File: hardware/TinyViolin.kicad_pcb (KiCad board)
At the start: 2 copper layers, 100 x 80 mm, 46 parts, among them J1 AVR-ISP-6, J2 503182-1852, SW1 SW_SPDT, SW2 Tactile, SW3 SW_Push, SW4 SW_Push, SW5 SW_Push, SW6 SW_Push, U1 ATmega328-PU, U2 TPS613222ADBVT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

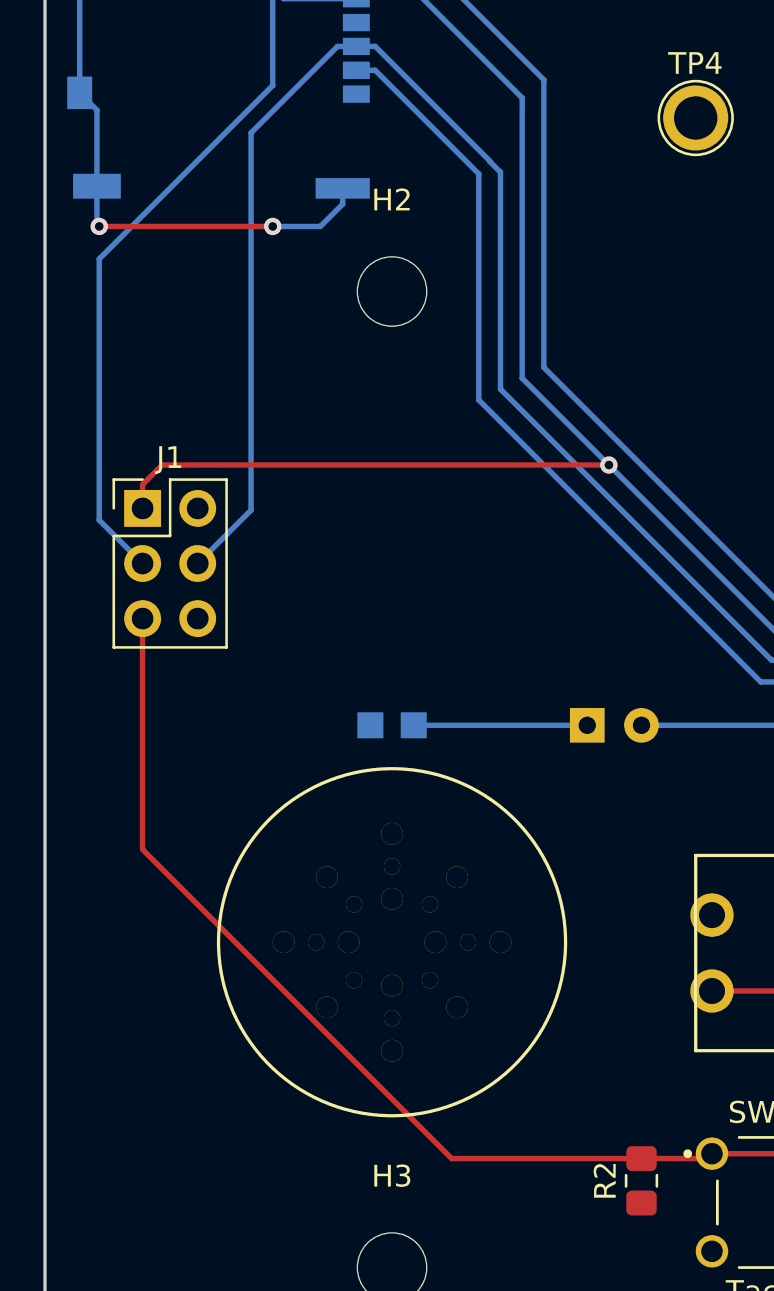
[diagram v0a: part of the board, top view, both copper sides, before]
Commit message: Moved icsp header up
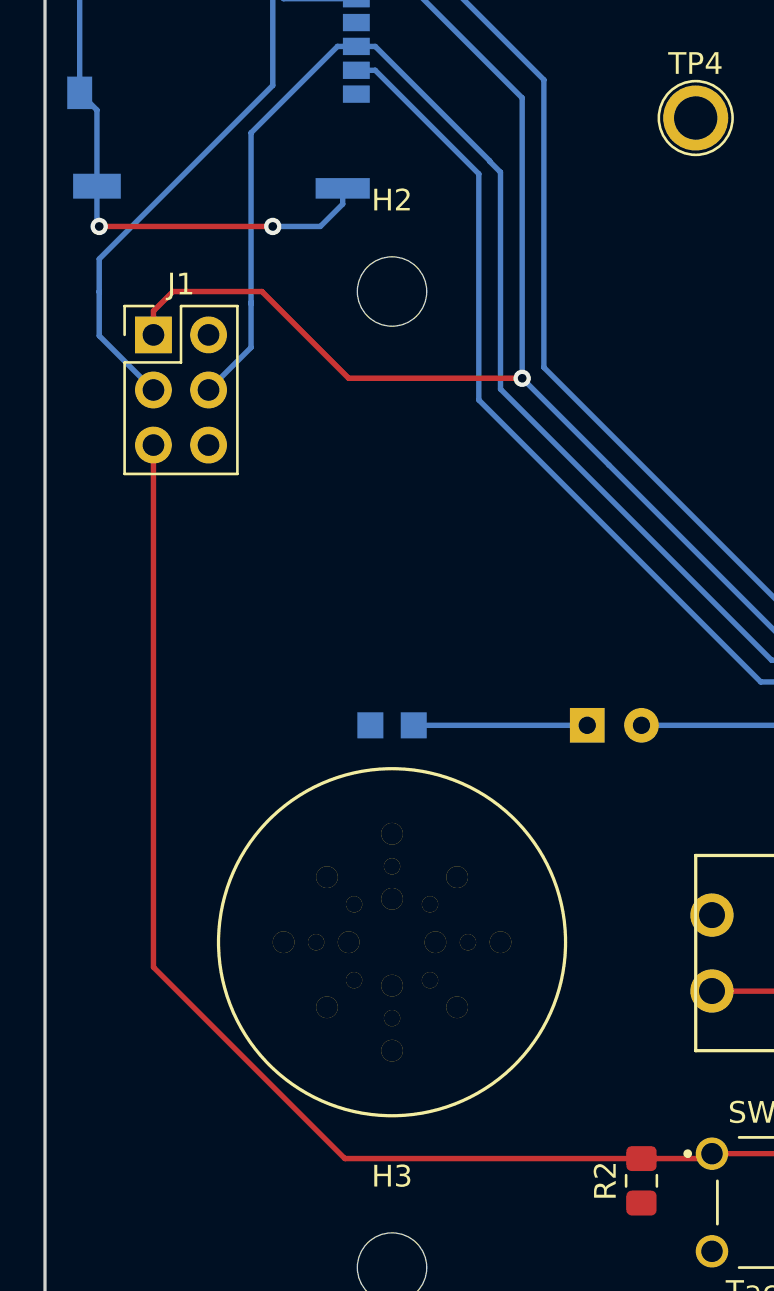
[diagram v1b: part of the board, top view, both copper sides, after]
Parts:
- moved J1 8.02 mm to (25.0, 52.0)
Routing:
- net /~RST: track 104.1 -> 115.3 mm
- net /MOSI: track 77.7 -> 69.6 mm
- net /SCK: track 101.9 -> 94.2 mm
- net /MISO: track 79.0 -> 76.1 mm
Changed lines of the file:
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@@
     (thickness 1.6)
     (drawings 4)
-    (tracks 158)
+    (tracks 163)
     (zones 0)
     (modules 46)
@@
   )
   (module Connector_PinHeader_2.54mm:PinHeader_2x03_P2.54mm_Vertical (layer F.Cu)
-    (at 24.5 60)
+    (at 25 52)
     (descr "Through hole straight pin header, 2x03, 2.54mm pitch, double rows")
     (tags "Through hole pin header THT 2x03 2.54mm double row")
@@
   (segment (start 33.485 38.7) (end 29.5 42.685) (width 0.25) (layer B.Cu) (net 1))
   (segment (start 34.355 38.7) (end 33.485 38.7) (width 0.25) (layer B.Cu) (net 1))
-  (segment (start 29.5 60.08) (end 27.04 62.54) (width 0.25) (layer B.Cu) (net 1))
-  (segment (start 29.5 42.685) (end 29.5 60.08) (width 0.25) (layer B.Cu) (net 1))
+  (segment (start 29.5 50.58) (end 29.5 50.5) (width 0.25) (layer B.Cu) (net 1))
+  (segment (start 29.5 42.685) (end 29.5 50.5) (width 0.25) (layer B.Cu) (net 1))
+  (segment (start 27.54 54.54) (end 29.5 52.58) (width 0.25) (layer B.Cu) (net 1))
+  (segment (start 29.5 52.58) (end 29.5 50.5) (width 0.25) (layer B.Cu) (net 1))
   (via (at 95 62) (size 0.8) (drill 0.4) (layers F.Cu B.Cu) (net 11))
   (via (at 95 73) (size 0.8) (drill 0.4) (layers F.Cu B.Cu) (net 11))
@@
   (segment (start 42 54) (end 42 41.075) (width 0.25) (layer B.Cu) (net 5))
   (segment (start 42 41.075) (end 35.225 34.3) (width 0.25) (layer B.Cu) (net 5))
-  (segment (start 24.5 58.9) (end 25.4 58) (width 0.25) (layer F.Cu) (net 5))
-  (segment (start 24.5 60) (end 24.5 58.9) (width 0.25) (layer F.Cu) (net 5))
-  (segment (start 25.4 58) (end 46 58) (width 0.25) (layer F.Cu) (net 5))
   (segment (start 46 58) (end 42 54) (width 0.25) (layer B.Cu) (net 5))
-  (via (at 46 58) (size 0.8) (drill 0.4) (layers F.Cu B.Cu) (net 5))
+  (via (at 42 54) (size 0.8) (drill 0.4) (layers F.Cu B.Cu) (net 5))
+  (segment (start 42 54) (end 34 54) (width 0.25) (layer F.Cu) (net 5))
+  (segment (start 25 50.9) (end 25.9 50) (width 0.25) (layer F.Cu) (net 5))
+  (segment (start 25 52) (end 25 50.9) (width 0.25) (layer F.Cu) (net 5))
+  (segment (start 25.9 50) (end 30 50) (width 0.25) (layer F.Cu) (net 5))
+  (segment (start 34 54) (end 30 50) (width 0.25) (layer F.Cu) (net 5))
   (segment (start 69.64 70.12) (end 69.64 70.52) (width 0.25) (layer B.Cu) (net 6))
   (segment (start 69.64 69.72) (end 69.64 70.12) (width 0.25) (layer B.Cu) (net 6))
-  (segment (start 22.5 60.54) (end 24.5 62.54) (width 0.25) (layer B.Cu) (net 6))
-  (segment (start 22.5 48.5) (end 22.5 60.54) (width 0.25) (layer B.Cu) (net 6))
   (segment (start 33 32) (end 30.5 34.5) (width 0.25) (layer B.Cu) (net 6))
   (segment (start 34.760002 32) (end 33 32) (width 0.25) (layer B.Cu) (net 6))
@@
   (segment (start 30.5 36) (end 30.5 40.5) (width 0.25) (layer B.Cu) (net 6))
   (segment (start 30.5 40.5) (end 22.5 48.5) (width 0.25) (layer B.Cu) (net 6))
+  (segment (start 22.5 50.04) (end 22.5 50) (width 0.25) (layer B.Cu) (net 6))
+  (segment (start 22.5 48.5) (end 22.5 50) (width 0.25) (layer B.Cu) (net 6))
+  (segment (start 22.5 52.04) (end 25 54.54) (width 0.25) (layer B.Cu) (net 6))
+  (segment (start 22.5 50) (end 22.5 52.04) (width 0.25) (layer B.Cu) (net 6))
   (segment (start 79.8 61.05) (end 71.25 52.5) (width 0.25) (layer B.Cu) (net 7))
   (segment (start 79.8 62.5) (end 79.8 61.05) (width 0.25) (layer B.Cu) (net 7))
@@
   (segment (start 47.5 89.975) (end 50.525 89.975) (width 0.25) (layer F.Cu) (net 14))
   (segment (start 50.75 89.75) (end 57.25 89.75) (width 0.25) (layer F.Cu) (net 14))
-  (segment (start 46.7 89.975) (end 47.5 89.975) (width 0.25) (layer F.Cu) (net 14))
-  (segment (start 38.753998 89.975) (end 46.7 89.975) (width 0.25) (layer F.Cu) (net 14))
-  (segment (start 24.5 75.721002) (end 38.753998 89.975) (width 0.25) (layer F.Cu) (net 14))
-  (segment (start 24.5 65.58) (end 24.5 75.721002) (width 0.25) (layer F.Cu) (net 14))
   (segment (start 93.55 62.5) (end 94.5 63.45) (width 0.25) (layer B.Cu) (net 14))
   (segment (start 92.5 62.5) (end 93.55 62.5) (width 0.25) (layer B.Cu) (net 14))
@@
   (segment (start 67 80) (end 57.25 89.75) (width 0.25) (layer B.Cu) (net 14))
   (segment (start 86 80) (end 67 80) (width 0.25) (layer B.Cu) (net 14))
+  (segment (start 25 57.08) (end 25 81.150998) (width 0.25) (layer F.Cu) (net 14))
+  (segment (start 33.824002 89.975) (end 25 81.150998) (width 0.25) (layer F.Cu) (net 14))
+  (segment (start 47.5 89.975) (end 33.824002 89.975) (width 0.25) (layer F.Cu) (net 14))
   (segment (start 98.475 70) (end 103.5 70) (width 0.25) (layer F.Cu) (net 15))
   (segment (start 97 68.525) (end 98.475 70) (width 0.25) (layer F.Cu) (net 15))

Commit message: Fixed labels
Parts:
- J1: value AVR-ISP-6 -> ICSP
- U2: value TPS613222ADBVT -> BOOST
- U3: value MIC5504-3.3YM5 -> REG
- moved C10 2.50 mm to (47.5, 70.0), turned to 180 degrees
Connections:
- C10 pad 1: Net-(C10-Pad1) -> /SPEAKER
- C10 pad 2: /SPEAKER -> Net-(C10-Pad2)
- LS1 pad 1: Net-(C10-Pad1) -> Net-(C10-Pad2)
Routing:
- net Net-(C10-Pad2): track 0.00 -> 8.00 mm
- net Net-(C10-Pad1): track 8.00 -> 0.00 mm
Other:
- board text added: "+"
- board text added: "-"
- board text added: "."
- board text added: "Tiny Violin MM v1.0"

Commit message: Wrote code for buttons and leds
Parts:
- U1: footprint Package_DIP:DIP-28_W7.62mm_Socket_LongPads -> Package_DIP:DIP-28_W7.62mm_LongPads

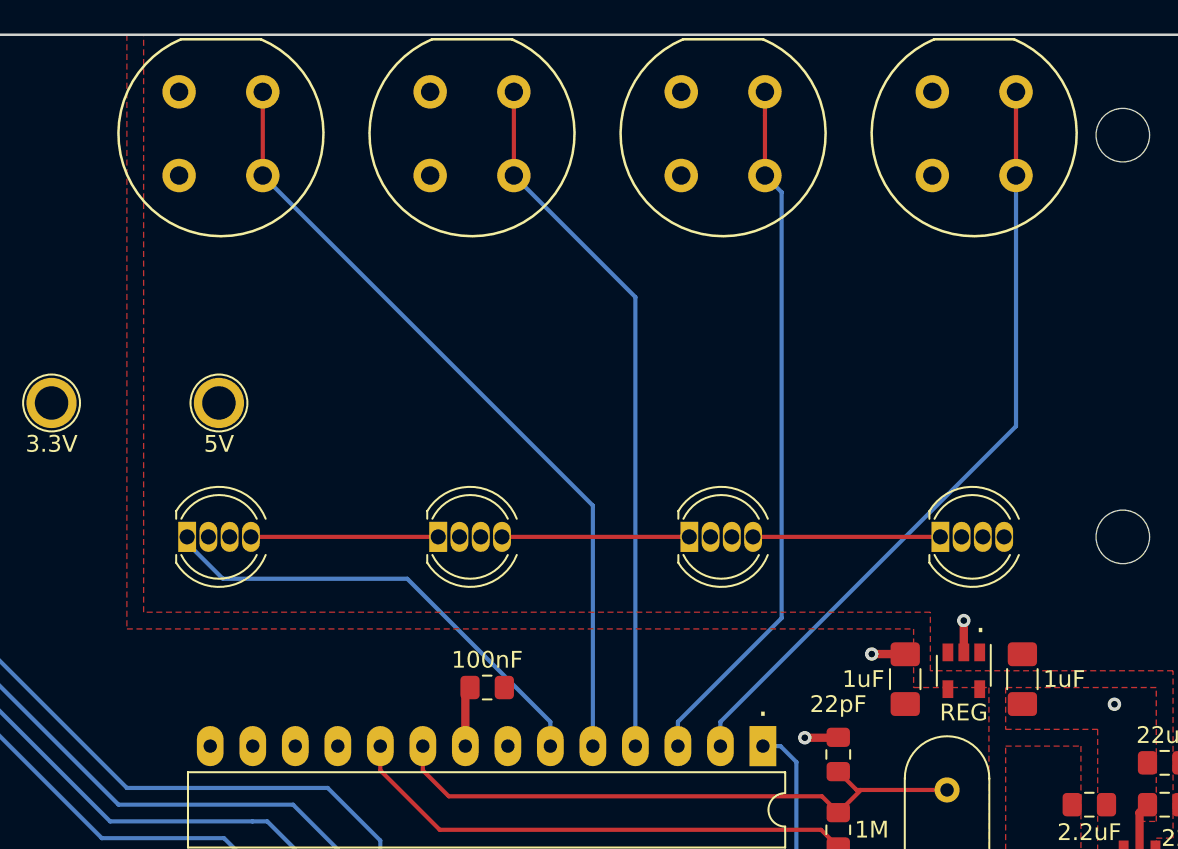
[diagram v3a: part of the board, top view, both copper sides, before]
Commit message: Moved holes and leds 1mm to the left
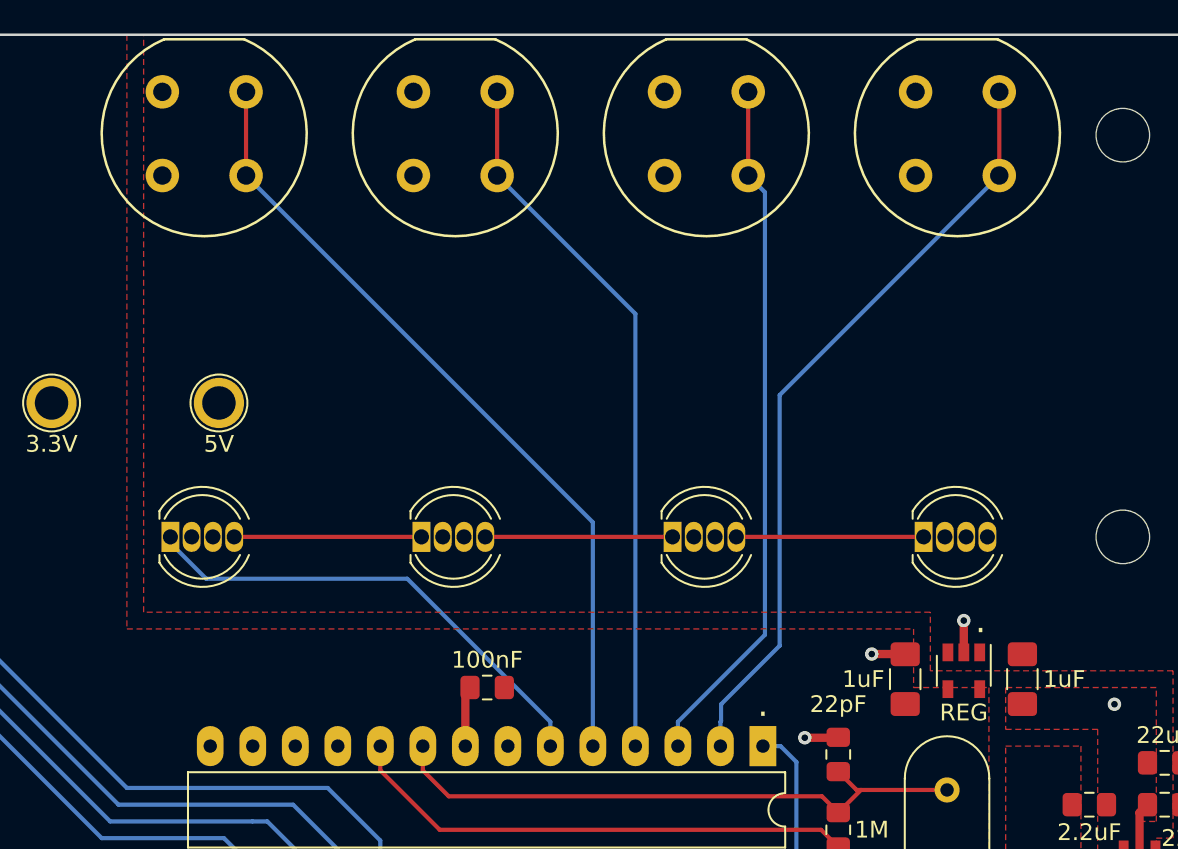
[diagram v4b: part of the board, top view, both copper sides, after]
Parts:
- moved D3 1.00 mm to (57.1, 50.0)
- moved D4 1.00 mm to (72.1, 50.0)
- moved D5 1.00 mm to (87.1, 50.0)
- moved D6 1.00 mm to (102.1, 50.0)
- moved SW3 1.00 mm to (61.5, 23.5)
- moved SW4 1.00 mm to (76.5, 23.5)
- moved SW5 1.00 mm to (91.5, 23.5)
- moved SW6 1.00 mm to (106.5, 23.5)
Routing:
- net /LEDS: track 27.9 -> 28.9 mm
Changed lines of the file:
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@@
     (thickness 1.6)
     (drawings 11)
-    (tracks 163)
+    (tracks 164)
     (zones 0)
     (modules 46)
@@
   )
   (module D6:D6 (layer F.Cu)
-    (at 107.5 23.5 270)
+    (at 106.5 23.5 270)
     (fp_text reference SW6 (at 6 9.5 270) (layer F.SilkS) hide
       (effects (font (size 1 1) (thickness 0.15)))
@@
   )
   (module D6:D6 (layer F.Cu)
-    (at 92.5 23.5 270)
+    (at 91.5 23.5 270)
     (fp_text reference SW5 (at 6 9.5 270) (layer F.SilkS) hide
       (effects (font (size 1 1) (thickness 0.15)))
@@
   )
   (module D6:D6 (layer F.Cu)
-    (at 77.5 23.5 270)
+    (at 76.5 23.5 270)
     (fp_text reference SW4 (at 6 9.5 270) (layer F.SilkS) hide
       (effects (font (size 1 1) (thickness 0.15)))
@@
   )
   (module D6:D6 (layer F.Cu)
-    (at 62.5 23.5 270)
+    (at 61.5 23.5 270)
     (fp_text reference SW3 (at 6 9.5 270) (layer F.SilkS) hide
       (effects (font (size 1 1) (thickness 0.15)))
@@
   )
   (module LED_THT:LED_D5.0mm-4_RGB (layer F.Cu)
-    (at 73.1 50)
+    (at 72.1 50)
     (descr "LED, diameter 5.0mm, 2 pins, diameter 5.0mm, 3 pins, diameter 5.0mm, 4 pins, http://www.kingbright.com/attachments/file/psearch/000/00/00/L-154A4SUREQBFZGEW(Ver.9A).pdf")
     (tags "LED diameter 5.0mm 2 pins diameter 5.0mm 3 pins diameter 5.0mm 4 pins RGB RGBLED")
@@
   )
   (module LED_THT:LED_D5.0mm-4_RGB (layer F.Cu)
-    (at 58.1 50)
+    (at 57.1 50)
     (descr "LED, diameter 5.0mm, 2 pins, diameter 5.0mm, 3 pins, diameter 5.0mm, 4 pins, http://www.kingbright.com/attachments/file/psearch/000/00/00/L-154A4SUREQBFZGEW(Ver.9A).pdf")
     (tags "LED diameter 5.0mm 2 pins diameter 5.0mm 3 pins diameter 5.0mm 4 pins RGB RGBLED")
@@
   )
   (module LED_THT:LED_D5.0mm-4_RGB (layer F.Cu)
-    (at 103.1 50)
+    (at 102.1 50)
     (descr "LED, diameter 5.0mm, 2 pins, diameter 5.0mm, 3 pins, diameter 5.0mm, 4 pins, http://www.kingbright.com/attachments/file/psearch/000/00/00/L-154A4SUREQBFZGEW(Ver.9A).pdf")
     (tags "LED diameter 5.0mm 2 pins diameter 5.0mm 3 pins diameter 5.0mm 4 pins RGB RGBLED")
@@
   )
   (module LED_THT:LED_D5.0mm-4_RGB (layer F.Cu)
-    (at 88.1 50)
+    (at 87.1 50)
     (descr "LED, diameter 5.0mm, 2 pins, diameter 5.0mm, 3 pins, diameter 5.0mm, 4 pins, http://www.kingbright.com/attachments/file/psearch/000/00/00/L-154A4SUREQBFZGEW(Ver.9A).pdf")
     (tags "LED diameter 5.0mm 2 pins diameter 5.0mm 3 pins diameter 5.0mm 4 pins RGB RGBLED")
@@
   (segment (start 22.5 52.04) (end 25 54.54) (width 0.25) (layer B.Cu) (net 6))
   (segment (start 22.5 50) (end 22.5 52.04) (width 0.25) (layer B.Cu) (net 6))
+  (segment (start 58.1 50.365) (end 58.1 50) (width 0.25) (layer B.Cu) (net 3))
+  (segment (start 57.1 50.365) (end 57.1 50) (width 0.25) (layer B.Cu) (net 7))
+  (segment (start 59.235 52.5) (end 57.1 50.365) (width 0.25) (layer B.Cu) (net 7))
+  (segment (start 71.25 52.5) (end 59.235 52.5) (width 0.25) (layer B.Cu) (net 7))
   (segment (start 79.8 61.05) (end 71.25 52.5) (width 0.25) (layer B.Cu) (net 7))
   (segment (start 79.8 62.5) (end 79.8 61.05) (width 0.25) (layer B.Cu) (net 7))
-  (segment (start 58.1 50.365) (end 58.1 50) (width 0.25) (layer B.Cu) (net 7))
-  (segment (start 60.235 52.5) (end 58.1 50.365) (width 0.25) (layer B.Cu) (net 7))
-  (segment (start 71.25 52.5) (end 60.235 52.5) (width 0.25) (layer B.Cu) (net 7))
   (segment (start 79.8 70.52) (end 79.8 70.12) (width 0.25) (layer F.Cu) (net 8))
   (segment (start 68.07 82.25) (end 79.8 70.52) (width 0.25) (layer F.Cu) (net 8))
@@
   (segment (start 95.975 67.5) (end 97 68.525) (width 0.25) (layer F.Cu) (net 14))
   (segment (start 73.19 67.5) (end 95.975 67.5) (width 0.25) (layer F.Cu) (net 14))
-  (segment (start 107.619299 29.825612) (end 107.619299 28.411399) (width 0.25) (layer B.Cu) (net 16))
-  (segment (start 107.619299 43.390701) (end 107.619299 29.825612) (width 0.25) (layer B.Cu) (net 16))
-  (segment (start 89.96 61.05) (end 107.619299 43.390701) (width 0.25) (layer B.Cu) (net 16))
+  (segment (start 89.96 61.05) (end 90 61.01) (width 0.25) (layer B.Cu) (net 16))
   (segment (start 89.96 62.5) (end 89.96 61.05) (width 0.25) (layer B.Cu) (net 16))
-  (segment (start 107.619299 24.825612) (end 107.619299 28.411399) (width 0.25) (layer F.Cu) (net 16))
-  (segment (start 107.619299 23.411399) (end 107.619299 24.825612) (width 0.25) (layer F.Cu) (net 16))
+  (segment (start 90 61.01) (end 90 60) (width 0.25) (layer B.Cu) (net 16))
+  (segment (start 90 60) (end 93.5 56.5) (width 0.25) (layer B.Cu) (net 16))
+  (segment (start 93.5 41.530698) (end 106.619299 28.411399) (width 0.25) (layer B.Cu) (net 16))
+  (segment (start 93.5 56.5) (end 93.5 41.530698) (width 0.25) (layer B.Cu) (net 16))
+  (segment (start 106.619299 28.411399) (end 106.619299 23.411399) (width 0.25) (layer F.Cu) (net 16))
   (segment (start 67.1 62.5) (end 67.1 62.9) (width 0.25) (layer F.Cu) (net 17))
-  (segment (start 82.34 48.1321) (end 62.619299 28.411399) (width 0.25) (layer B.Cu) (net 25))
-  (segment (start 82.34 62.5) (end 82.34 48.1321) (width 0.25) (layer B.Cu) (net 25))
-  (segment (start 62.619299 23.411399) (end 62.619299 28.411399) (width 0.25) (layer F.Cu) (net 25))
-  (segment (start 84.88 35.6721) (end 77.619299 28.411399) (width 0.25) (layer B.Cu) (net 26))
-  (segment (start 84.88 62.5) (end 84.88 35.6721) (width 0.25) (layer B.Cu) (net 26))
-  (segment (start 77.619299 23.411399) (end 77.619299 28.411399) (width 0.25) (layer F.Cu) (net 26))
-  (segment (start 93.619298 29.411398) (end 92.619299 28.411399) (width 0.25) (layer B.Cu) (net 27))
-  (segment (start 93.619298 54.850702) (end 93.619298 29.411398) (width 0.25) (layer B.Cu) (net 27))
-  (segment (start 87.42 61.05) (end 93.619298 54.850702) (width 0.25) (layer B.Cu) (net 27))
+  (segment (start 82.34 49.1321) (end 82.34 62.5) (width 0.25) (layer B.Cu) (net 25))
+  (segment (start 61.619299 28.411399) (end 82.34 49.1321) (width 0.25) (layer B.Cu) (net 25))
+  (segment (start 61.619299 28.411399) (end 61.619299 23.411399) (width 0.25) (layer F.Cu) (net 25))
+  (segment (start 84.88 36.6721) (end 76.619299 28.411399) (width 0.25) (layer B.Cu) (net 26))
+  (segment (start 84.88 62.5) (end 84.88 36.6721) (width 0.25) (layer B.Cu) (net 26))
+  (segment (start 76.619299 28.411399) (end 76.619299 23.411399) (width 0.25) (layer F.Cu) (net 26))
+  (segment (start 92.619298 29.411398) (end 91.619299 28.411399) (width 0.25) (layer B.Cu) (net 27))
+  (segment (start 92.619298 55.850702) (end 92.619298 29.411398) (width 0.25) (layer B.Cu) (net 27))
+  (segment (start 87.42 61.05) (end 92.619298 55.850702) (width 0.25) (layer B.Cu) (net 27))
   (segment (start 87.42 62.5) (end 87.42 61.05) (width 0.25) (layer B.Cu) (net 27))
-  (segment (start 92.619299 24.825612) (end 92.619299 28.411399) (width 0.25) (layer F.Cu) (net 27))
-  (segment (start 92.619299 23.411399) (end 92.619299 24.825612) (width 0.25) (layer F.Cu) (net 27))
-  (segment (start 76.91 50) (end 88.1 50) (width 0.25) (layer F.Cu) (net 29))
-  (segment (start 91.91 50) (end 103.1 50) (width 0.25) (layer F.Cu) (net 30))
-  (segment (start 61.91 50) (end 73.1 50) (width 0.25) (layer F.Cu) (net 32))
+  (segment (start 91.619299 28.411399) (end 91.619299 23.411399) (width 0.25) (layer F.Cu) (net 27))
+  (segment (start 75.91 50) (end 87.1 50) (width 0.25) (layer F.Cu) (net 29))
+  (segment (start 90.91 50) (end 102.1 50) (width 0.25) (layer F.Cu) (net 30))
+  (segment (start 60.91 50) (end 72.1 50) (width 0.25) (layer F.Cu) (net 32))
   (segment (start 22.425 33.06) (end 21.6 33.06) (width 0.25) (layer B.Cu) (net 38))
   (segment (start 22.690002 33.06) (end 22.425 33.06) (width 0.25) (layer B.Cu) (net 38))
